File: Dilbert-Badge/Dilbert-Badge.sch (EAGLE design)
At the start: 5 parts

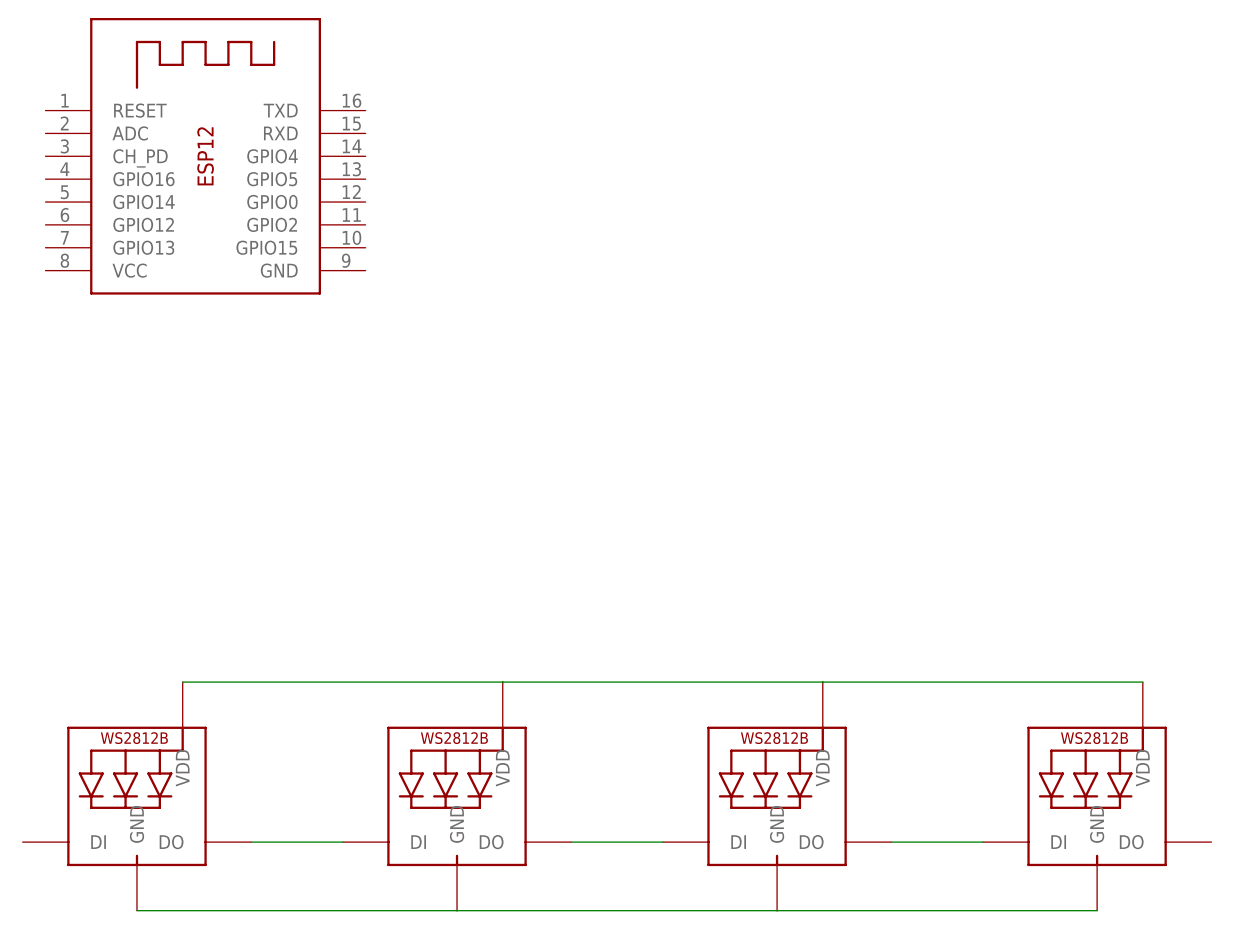
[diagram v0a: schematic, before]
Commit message: add switches, initial layout
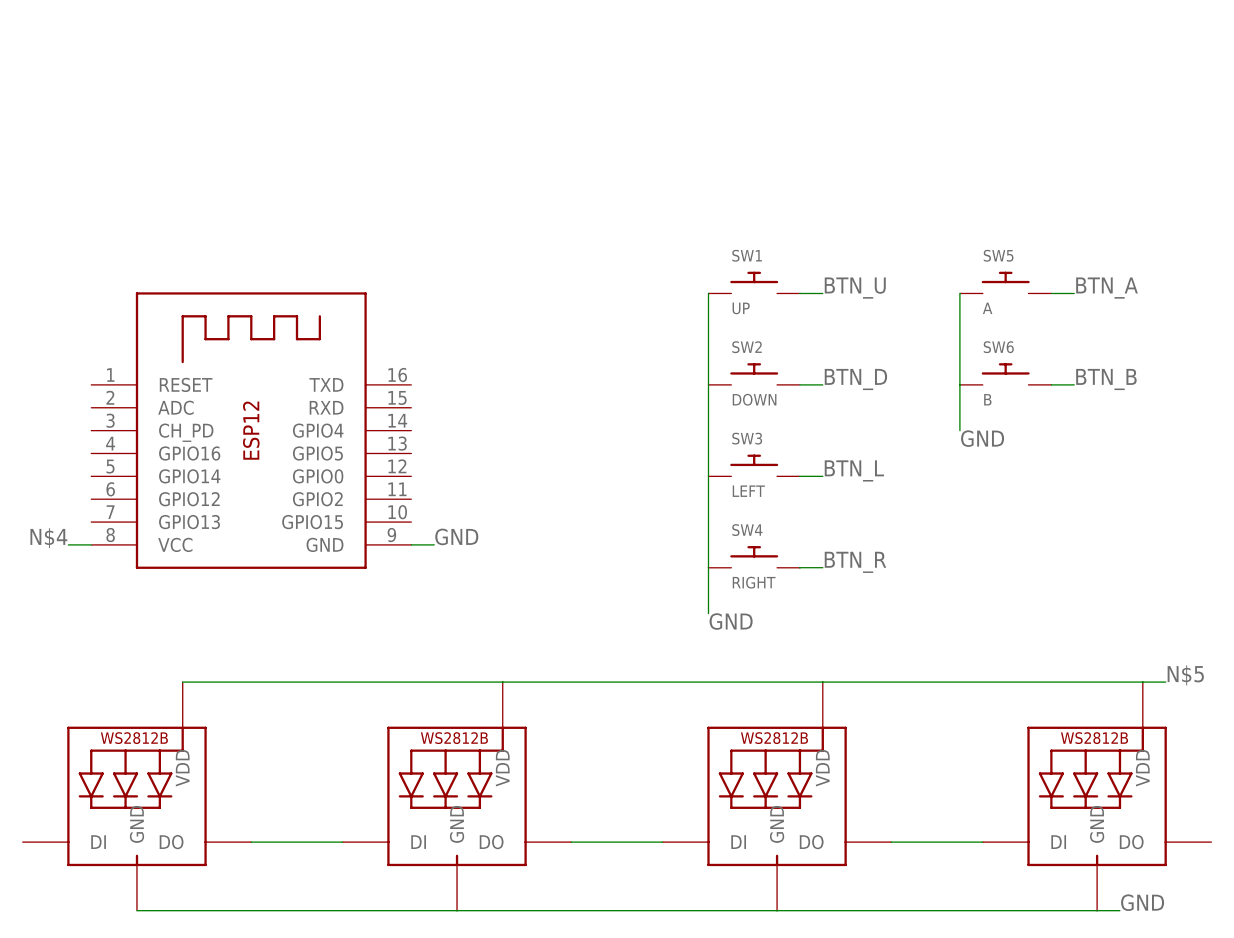
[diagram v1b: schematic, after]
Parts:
- added SW1: UP, adafruit:SWITCH_PUSHBUTTONEVQ-PE
- added SW2: DOWN, adafruit:SWITCH_PUSHBUTTONEVQ-PE
- added SW3: LEFT, adafruit:SWITCH_PUSHBUTTONEVQ-PE
- added SW4: RIGHT, adafruit:SWITCH_PUSHBUTTONEVQ-PE
- added SW5: A, adafruit:SWITCH_PUSHBUTTONEVQ-PE
- added SW6: B, adafruit:SWITCH_PUSHBUTTONEVQ-PE
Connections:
- removed net N$6: LED1.GND, LED2.GND, LED3.GND, LED4.GND
- new net BTN_A: SW5.P$2
- new net BTN_B: SW6.P$2
- new net BTN_D: SW2.P$2
- new net BTN_L: SW3.P$2
- new net BTN_R: SW4.P$2
- new net BTN_U: SW1.P$2
- new net GND: LED1.GND, LED2.GND, LED3.GND, LED4.GND, SW1.P$1, SW4.P$1, SW5.P$1, SW6.P$1, X1.GND
- new net N$4: X1.VCC
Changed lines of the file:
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@@
 <part name="LED4" library="adafruit" deviceset="WS2812B" device="5050"/>
 <part name="X1" library="adafruit" deviceset="ESP-12" device=""/>
+<part name="SW1" library="adafruit" deviceset="SWITCH_PUSHBUTTON" device="EVQ-PE" value="UP"/>
+<part name="SW2" library="adafruit" deviceset="SWITCH_PUSHBUTTON" device="EVQ-PE" value="DOWN"/>
+<part name="SW3" library="adafruit" deviceset="SWITCH_PUSHBUTTON" device="EVQ-PE" value="LEFT"/>
+<part name="SW4" library="adafruit" deviceset="SWITCH_PUSHBUTTON" device="EVQ-PE" value="RIGHT"/>
+<part name="SW5" library="adafruit" deviceset="SWITCH_PUSHBUTTON" device="EVQ-PE" value="A"/>
+<part name="SW6" library="adafruit" deviceset="SWITCH_PUSHBUTTON" device="EVQ-PE" value="B"/>
 </parts>
 <sheets>
@@
 <instance part="LED3" gate="G$1" x="101.6" y="35.56"/>
 <instance part="LED4" gate="G$1" x="137.16" y="35.56"/>
-<instance part="X1" gate="G$1" x="38.1" y="109.22"/>
+<instance part="X1" gate="G$1" x="43.18" y="78.74"/>
+<instance part="SW1" gate="G$1" x="99.06" y="93.98"/>
+<instance part="SW2" gate="G$1" x="99.06" y="83.82"/>
+<instance part="SW3" gate="G$1" x="99.06" y="73.66"/>
+<instance part="SW4" gate="G$1" x="99.06" y="63.5"/>
+<instance part="SW5" gate="G$1" x="127" y="93.98"/>
+<instance part="SW6" gate="G$1" x="127" y="83.82"/>
 </instances>
 <busses>
@@
 <wire x1="35.56" y1="50.8" x2="71.12" y2="50.8" width="0.1524" layer="91"/>
 <wire x1="106.68" y1="50.8" x2="71.12" y2="50.8" width="0.1524" layer="91"/>
+<wire x1="144.78" y1="50.8" x2="142.24" y2="50.8" width="0.1524" layer="91"/>
+<label x="144.78" y="50.8" size="1.778" layer="95"/>
 </segment>
 </net>
-<net name="N$6" class="0">
+<net name="GND" class="0">
+<segment>
+<pinref part="SW1" gate="G$1" pin="P$1"/>
+<pinref part="SW4" gate="G$1" pin="P$1"/>
+<wire x1="93.98" y1="93.98" x2="93.98" y2="63.5" width="0.1524" layer="91"/>
+<label x="93.98" y="58.42" size="1.778" layer="95" rot="MR180"/>
+<wire x1="93.98" y1="63.5" x2="93.98" y2="58.42" width="0.1524" layer="91"/>
+</segment>
+<segment>
+<pinref part="SW5" gate="G$1" pin="P$1"/>
+<pinref part="SW6" gate="G$1" pin="P$1"/>
+<wire x1="121.92" y1="93.98" x2="121.92" y2="83.82" width="0.1524" layer="91"/>
+<label x="121.92" y="78.74" size="1.778" layer="95" rot="MR180"/>
+<wire x1="121.92" y1="83.82" x2="121.92" y2="78.74" width="0.1524" layer="91"/>
+</segment>
 <segment>
 <pinref part="LED1" gate="G$1" pin="GND"/>
@@
 <pinref part="LED4" gate="G$1" pin="GND"/>
 <wire x1="101.6" y1="25.4" x2="137.16" y2="25.4" width="0.1524" layer="91"/>
+<wire x1="139.7" y1="25.4" x2="137.16" y2="25.4" width="0.1524" layer="91"/>
+<label x="139.7" y="25.4" size="1.778" layer="95"/>
+</segment>
+<segment>
+<pinref part="X1" gate="G$1" pin="GND"/>
+<wire x1="60.96" y1="66.04" x2="63.5" y2="66.04" width="0.1524" layer="91"/>
+<label x="63.5" y="66.04" size="1.778" layer="95"/>
 </segment>
 </net>
+<net name="BTN_U" class="0">
+<segment>
+<pinref part="SW1" gate="G$1" pin="P$2"/>
+<wire x1="106.68" y1="93.98" x2="104.14" y2="93.98" width="0.1524" layer="91"/>
+<label x="106.68" y="93.98" size="1.778" layer="95"/>
+</segment>
+</net>
+<net name="BTN_D" class="0">
+<segment>
+<pinref part="SW2" gate="G$1" pin="P$2"/>
+<wire x1="106.68" y1="83.82" x2="104.14" y2="83.82" width="0.1524" layer="91"/>
+<label x="106.68" y="83.82" size="1.778" layer="95"/>
+</segment>
+</net>
+<net name="BTN_L" class="0">
+<segment>
+<pinref part="SW3" gate="G$1" pin="P$2"/>
+<wire x1="106.68" y1="73.66" x2="104.14" y2="73.66" width="0.1524" layer="91"/>
+<label x="106.68" y="73.66" size="1.778" layer="95"/>
+</segment>
+</net>
+<net name="BTN_R" class="0">
+<segment>
+<pinref part="SW4" gate="G$1" pin="P$2"/>
+<wire x1="106.68" y1="63.5" x2="104.14" y2="63.5" width="0.1524" layer="91"/>
+<label x="106.68" y="63.5" size="1.778" layer="95"/>
+</segment>
+</net>
+<net name="BTN_A" class="0">
+<segment>
+<pinref part="SW5" gate="G$1" pin="P$2"/>
+<wire x1="134.62" y1="93.98" x2="132.08" y2="93.98" width="0.1524" layer="91"/>
+<label x="134.62" y="93.98" size="1.778" layer="95"/>
+</segment>
+</net>
+<net name="BTN_B" class="0">
+<segment>
+<pinref part="SW6" gate="G$1" pin="P$2"/>
+<wire x1="134.62" y1="83.82" x2="132.08" y2="83.82" width="0.1524" layer="91"/>
+<label x="134.62" y="83.82" size="1.778" layer="95"/>
+</segment>
+</net>
+<net name="N$4" class="0">
+<segment>
+<pinref part="X1" gate="G$1" pin="VCC"/>
+<wire x1="22.86" y1="66.04" x2="25.4" y2="66.04" width="0.1524" layer="91"/>
+<label x="22.86" y="66.04" size="1.778" layer="95" rot="MR0"/>
+</segment>
+</net>

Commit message: a little more work
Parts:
- added J1: I2C, SparkFun-Connectors:M04PTH
- added J2: UART, SparkFun-Connectors:M06SILK_FEMALE_PTH
- added J3: (no value), SparkFun-Connectors:M03PTH
- added J4, J5: (no value), SparkFun-Connectors:M08NO_SILK_FEMALE_PTH
- added SW7: RESET, adafruit:SWITCH_PUSHBUTTONEVQ-PE
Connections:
- new net LED_IN: J5.7, LED1.DI, X1.GPIO15
- new net LED_OUT: J3.3, LED4.DO
- new net N$10: J4.2, X1.GPIO13
- new net N$11: J4.3, X1.GPIO12
- new net N$12: J5.3, X1.GPIO4
- new net N$13: J5.6, X1.GPIO2
- new net N$6: J4.6, X1.CH_PD
- new net N$7: J4.5, X1.GPIO16
- new net N$8: J4.8, X1.RESET
- new net N$9: J4.4, X1.GPIO14
- new net SCL: J1.4, J5.5, X1.GPIO0
- new net SDA: J1.3, J5.4, X1.GPIO5
- new net UART_CTS: J2.5
- new net UART_DTR: J2.1
- new net UART_RX: J2.3, J5.2, X1.RXD
- new net UART_TX: J2.2, J5.1, X1.TXD
- new net VCC: J1.2, J2.4, J3.2, J4.1, X1.VCC
- net GND: now also J1.1, J2.6, J3.1, J5.8, SW2.P$1, SW3.P$1, SW7.P$1
- net N$4: now also J4.7, X1.ADC; no longer X1.VCC
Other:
- moved on the sheet: SW1, SW2, SW3, SW4, SW5, SW6

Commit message: add IO expander, more general layout
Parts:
- added IC1: MCP23017SO, adafruit:MCP23017SO
- added J6: IO_B, SparkFun-Connectors:M08
- added J7: IO_A, SparkFun-Connectors:M08
- added LOGO1: OSHW-LOGOL, SparkFun-Aesthetics:OSHW-LOGOL
- added SW8: SWD, adafruit:SWITCH_PUSHBUTTONEVQ-PE
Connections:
- removed net N$5: LED1.VDD, LED2.VDD, LED3.VDD, LED4.VDD
- new net N$14: IC1.GPB0, J6.1
- new net N$15: IC1.GPB1, J6.2
- new net N$16: IC1.GPB7, J6.8
- new net N$17: IC1.GPB6, J6.7
- new net N$18: IC1.GPB5, J6.6
- new net N$19: IC1.GPB4, J6.5
- new net N$20: IC1.GPB3, J6.4
- new net N$21: IC1.GPB2, J6.3
- new net N$22: IC1.GPA7, J7.8
- new net N$23: IC1.GPA6, J7.7
- new net RESET: J4.8, SW7.P$2, X1.RESET
- net BTN_A: now also IC1.GPA4, J7.5
- net BTN_B: now also IC1.GPA5, J7.6
- net BTN_D: now also IC1.GPA1, J7.2
- net BTN_L: now also IC1.GPA2, J7.3
- net BTN_R: now also IC1.GPA3, J7.4
- net BTN_U: now also IC1.GPA0, J7.1
- net GND: now also IC1.VSS, SW8.P$1
- net N$8: now also SW8.P$2; no longer J4.8, X1.RESET
- net SCL: now also IC1.SCL
- net SDA: now also IC1.SDA
- net VCC: now also IC1.VDD, LED1.VDD, LED2.VDD, LED3.VDD, LED4.VDD
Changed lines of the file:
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@@
 <part name="J5" library="SparkFun-Connectors" deviceset="M08" device="NO_SILK_FEMALE_PTH"/>
 <part name="SW7" library="adafruit" deviceset="SWITCH_PUSHBUTTON" device="EVQ-PE" value="RESET"/>
+<part name="IC1" library="adafruit" deviceset="MCP23017" device="SO"/>
+<part name="SW8" library="adafruit" deviceset="SWITCH_PUSHBUTTON" device="EVQ-PE" value="SWD"/>
+<part name="J6" library="SparkFun-Connectors" deviceset="M08" device="" value="IO_B"/>
+<part name="J7" library="SparkFun-Connectors" deviceset="M08" device="" value="IO_A"/>
+<part name="LOGO1" library="SparkFun-Aesthetics" deviceset="OSHW-LOGO" device="L"/>
 </parts>
 <sheets>
@@
 <instance part="J5" gate="G$1" x="127" y="73.66" rot="R180"/>
 <instance part="SW7" gate="G$1" x="109.22" y="144.78" rot="R90"/>
+<instance part="IC1" gate="G$1" x="200.66" y="48.26"/>
+<instance part="SW8" gate="G$1" x="132.08" y="144.78" rot="R90"/>
+<instance part="J6" gate="G$1" x="231.14" y="38.1" rot="R180"/>
+<instance part="J7" gate="G$1" x="246.38" y="60.96" rot="R180"/>
+<instance part="LOGO1" gate="G$1" x="12.7" y="10.16"/>
 </instances>
 <busses>
@@
 <pinref part="LED4" gate="G$1" pin="DI"/>
 <wire x1="114.3" y1="33.02" x2="124.46" y2="33.02" width="0.1524" layer="91"/>
-</segment>
-</net>
-<net name="N$5" class="0">
-<segment>
-<pinref part="LED3" gate="G$1" pin="VDD"/>
-<pinref part="LED4" gate="G$1" pin="VDD"/>
-<wire x1="106.68" y1="50.8" x2="142.24" y2="50.8" width="0.1524" layer="91"/>
-<pinref part="LED1" gate="G$1" pin="VDD"/>
-<pinref part="LED2" gate="G$1" pin="VDD"/>
-<wire x1="35.56" y1="50.8" x2="71.12" y2="50.8" width="0.1524" layer="91"/>
-<wire x1="106.68" y1="50.8" x2="71.12" y2="50.8" width="0.1524" layer="91"/>
-<wire x1="144.78" y1="50.8" x2="142.24" y2="50.8" width="0.1524" layer="91"/>
-<label x="144.78" y="50.8" size="1.778" layer="95"/>
 </segment>
 </net>
@@
 <label x="109.22" y="134.62" size="1.778" layer="95" rot="MR180"/>
 </segment>
+<segment>
+<pinref part="IC1" gate="G$1" pin="VSS"/>
+<wire x1="185.42" y1="27.94" x2="187.96" y2="27.94" width="0.1524" layer="91"/>
+<label x="185.42" y="27.94" size="1.778" layer="95" rot="MR0"/>
+</segment>
+<segment>
+<pinref part="SW8" gate="G$1" pin="P$1"/>
+<wire x1="132.08" y1="139.7" x2="132.08" y2="134.62" width="0.1524" layer="91"/>
+<label x="132.08" y="134.62" size="1.778" layer="95" rot="MR180"/>
+</segment>
 </net>
 <net name="BTN_U" class="0">
@@
 <label x="48.26" y="170.18" size="1.778" layer="95"/>
 </segment>
+<segment>
+<pinref part="IC1" gate="G$1" pin="GPA0"/>
+<label x="215.9" y="68.58" size="1.778" layer="95"/>
+<pinref part="J7" gate="G$1" pin="1"/>
+<wire x1="213.36" y1="68.58" x2="241.3" y2="68.58" width="0.1524" layer="91"/>
+</segment>
 </net>
 <net name="BTN_D" class="0">
@@
 <label x="48.26" y="160.02" size="1.778" layer="95"/>
 </segment>
+<segment>
+<pinref part="IC1" gate="G$1" pin="GPA1"/>
+<label x="215.9" y="66.04" size="1.778" layer="95"/>
+<pinref part="J7" gate="G$1" pin="2"/>
+<wire x1="241.3" y1="66.04" x2="213.36" y2="66.04" width="0.1524" layer="91"/>
+</segment>
 </net>
 <net name="BTN_L" class="0">
@@
 <label x="48.26" y="149.86" size="1.778" layer="95"/>
 </segment>
+<segment>
+<pinref part="IC1" gate="G$1" pin="GPA2"/>
+<label x="215.9" y="63.5" size="1.778" layer="95"/>
+<pinref part="J7" gate="G$1" pin="3"/>
+<wire x1="213.36" y1="63.5" x2="241.3" y2="63.5" width="0.1524" layer="91"/>
+</segment>
 </net>
 <net name="BTN_R" class="0">
@@
 <label x="48.26" y="139.7" size="1.778" layer="95"/>
 </segment>
+<segment>
+<pinref part="IC1" gate="G$1" pin="GPA3"/>
+<label x="215.9" y="60.96" size="1.778" layer="95"/>
+<pinref part="J7" gate="G$1" pin="4"/>
+<wire x1="241.3" y1="60.96" x2="213.36" y2="60.96" width="0.1524" layer="91"/>
+</segment>
 </net>
 <net name="BTN_A" class="0">
@@
 <label x="81.28" y="149.86" size="1.778" layer="95"/>
 </segment>
+<segment>
+<pinref part="IC1" gate="G$1" pin="GPA4"/>
+<label x="215.9" y="58.42" size="1.778" layer="95"/>
+<pinref part="J7" gate="G$1" pin="5"/>
+<wire x1="213.36" y1="58.42" x2="241.3" y2="58.42" width="0.1524" layer="91"/>
+</segment>
 </net>
 <net name="BTN_B" class="0">
@@
 <label x="81.28" y="139.7" size="1.778" layer="95"/>
 </segment>
-</net>
-<net name="N$8" class="0">
+<segment>
+<pinref part="IC1" gate="G$1" pin="GPA5"/>
+<label x="215.9" y="55.88" size="1.778" layer="95"/>
+<pinref part="J7" gate="G$1" pin="6"/>
+<wire x1="213.36" y1="55.88" x2="241.3" y2="55.88" width="0.1524" layer="91"/>
+</segment>
+</net>
+<net name="RESET" class="0">
 <segment>
 <pinref part="X1" gate="G$1" pin="RESET"/>
 <pinref part="J4" gate="G$1" pin="8"/>
 <wire x1="45.72" y1="81.28" x2="66.04" y2="81.28" width="0.1524" layer="91"/>
+<label x="63.5" y="81.28" size="1.778" layer="95" rot="MR0"/>
+</segment>
+<segment>
+<pinref part="SW7" gate="G$1" pin="P$2"/>
+<wire x1="109.22" y1="154.94" x2="109.22" y2="152.4" width="0.1524" layer="91"/>
+<wire x1="109.22" y1="152.4" x2="109.22" y2="149.86" width="0.1524" layer="91"/>
+<wire x1="109.22" y1="152.4" x2="114.3" y2="152.4" width="0.1524" layer="91"/>
+<label x="114.3" y="152.4" size="1.778" layer="95"/>
 </segment>
 </net>
@@
 <label x="83.82" y="111.76" size="1.778" layer="95"/>
 </segment>
+<segment>
+<pinref part="IC1" gate="G$1" pin="SDA"/>
+<wire x1="185.42" y1="43.18" x2="187.96" y2="43.18" width="0.1524" layer="91"/>
+<label x="185.42" y="43.18" size="1.778" layer="95" rot="MR0"/>
+</segment>
 </net>
 <net name="SCL" class="0">
@@
 <label x="83.82" y="114.3" size="1.778" layer="95"/>
 </segment>
+<segment>
+<pinref part="IC1" gate="G$1" pin="SCL"/>
+<wire x1="185.42" y1="45.72" x2="187.96" y2="45.72" width="0.1524" layer="91"/>
+<label x="185.42" y="45.72" size="1.778" layer="95" rot="MR0"/>
+</segment>
 </net>
 <net name="UART_TX" class="0">
@@
 <label x="83.82" y="109.22" size="1.778" layer="95"/>
 </segment>
+<segment>
+<pinref part="IC1" gate="G$1" pin="VDD"/>
+<wire x1="185.42" y1="68.58" x2="187.96" y2="68.58" width="0.1524" layer="91"/>
+<label x="185.42" y="68.58" size="1.778" layer="95" rot="MR0"/>
+</segment>
+<segment>
+<pinref part="LED3" gate="G$1" pin="VDD"/>
+<pinref part="LED4" gate="G$1" pin="VDD"/>
+<wire x1="106.68" y1="50.8" x2="142.24" y2="50.8" width="0.1524" layer="91"/>
+<pinref part="LED1" gate="G$1" pin="VDD"/>
+<pinref part="LED2" gate="G$1" pin="VDD"/>
+<wire x1="35.56" y1="50.8" x2="71.12" y2="50.8" width="0.1524" layer="91"/>
+<wire x1="106.68" y1="50.8" x2="71.12" y2="50.8" width="0.1524" layer="91"/>
+<wire x1="144.78" y1="50.8" x2="142.24" y2="50.8" width="0.1524" layer="91"/>
+<label x="144.78" y="50.8" size="1.778" layer="95"/>
+</segment>
 </net>
 <net name="UART_DTR" class="0">
@@
 </segment>
 </net>
+<net name="N$8" class="0">
+<segment>
+<pinref part="SW8" gate="G$1" pin="P$2"/>
+<wire x1="132.08" y1="154.94" x2="132.08" y2="152.4" width="0.1524" layer="91"/>
+<wire x1="132.08" y1="152.4" x2="132.08" y2="149.86" width="0.1524" layer="91"/>
+<wire x1="132.08" y1="152.4" x2="137.16" y2="152.4" width="0.1524" layer="91"/>
+<label x="137.16" y="152.4" size="1.778" layer="95"/>
+</segment>
+</net>
+<net name="N$14" class="0">
+<segment>
+<pinref part="IC1" gate="G$1" pin="GPB0"/>
+<pinref part="J6" gate="G$1" pin="1"/>
+<wire x1="213.36" y1="45.72" x2="226.06" y2="45.72" width="0.1524" layer="91"/>
+</segment>
+</net>
+<net name="N$15" class="0">
+<segment>
+<pinref part="IC1" gate="G$1" pin="GPB1"/>
+<pinref part="J6" gate="G$1" pin="2"/>
+<wire x1="213.36" y1="43.18" x2="226.06" y2="43.18" width="0.1524" layer="91"/>
+</segment>
+</net>
+<net name="N$16" class="0">
+<segment>
+<pinref part="J6" gate="G$1" pin="8"/>
+<pinref part="IC1" gate="G$1" pin="GPB7"/>
+<wire x1="226.06" y1="27.94" x2="213.36" y2="27.94" width="0.1524" layer="91"/>
+</segment>
+</net>
+<net name="N$17" class="0">
+<segment>
+<pinref part="IC1" gate="G$1" pin="GPB6"/>
+<pinref part="J6" gate="G$1" pin="7"/>
+<wire x1="213.36" y1="30.48" x2="226.06" y2="30.48" width="0.1524" layer="91"/>
+</segment>
+</net>
+<net name="N$18" class="0">
+<segment>
+<pinref part="J6" gate="G$1" pin="6"/>
+<pinref part="IC1" gate="G$1" pin="GPB5"/>
+<wire x1="226.06" y1="33.02" x2="213.36" y2="33.02" width="0.1524" layer="91"/>
+</segment>
+</net>
+<net name="N$19" class="0">
+<segment>
+<pinref part="IC1" gate="G$1" pin="GPB4"/>
+<pinref part="J6" gate="G$1" pin="5"/>
+<wire x1="213.36" y1="35.56" x2="226.06" y2="35.56" width="0.1524" layer="91"/>
+</segment>
+</net>
+<net name="N$20" class="0">
+<segment>
+<pinref part="J6" gate="G$1" pin="4"/>
+<pinref part="IC1" gate="G$1" pin="GPB3"/>
+<wire x1="226.06" y1="38.1" x2="213.36" y2="38.1" width="0.1524" layer="91"/>
+</segment>
+</net>
+<net name="N$21" class="0">
+<segment>
+<pinref part="IC1" gate="G$1" pin="GPB2"/>
+<pinref part="J6" gate="G$1" pin="3"/>
+<wire x1="213.36" y1="40.64" x2="226.06" y2="40.64" width="0.1524" layer="91"/>
+</segment>
+</net>
+<net name="N$22" class="0">
+<segment>
+<pinref part="IC1" gate="G$1" pin="GPA7"/>
+<pinref part="J7" gate="G$1" pin="8"/>
+<wire x1="213.36" y1="50.8" x2="241.3" y2="50.8" width="0.1524" layer="91"/>
+</segment>
+</net>
+<net name="N$23" class="0">
+<segment>
+<pinref part="J7" gate="G$1" pin="7"/>
+<pinref part="IC1" gate="G$1" pin="GPA6"/>
+<wire x1="241.3" y1="53.34" x2="213.36" y2="53.34" width="0.1524" layer="91"/>
+</segment>
+</net>
